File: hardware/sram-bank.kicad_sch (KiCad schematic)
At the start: 6 parts, among them U1 NAND, U13 decoder

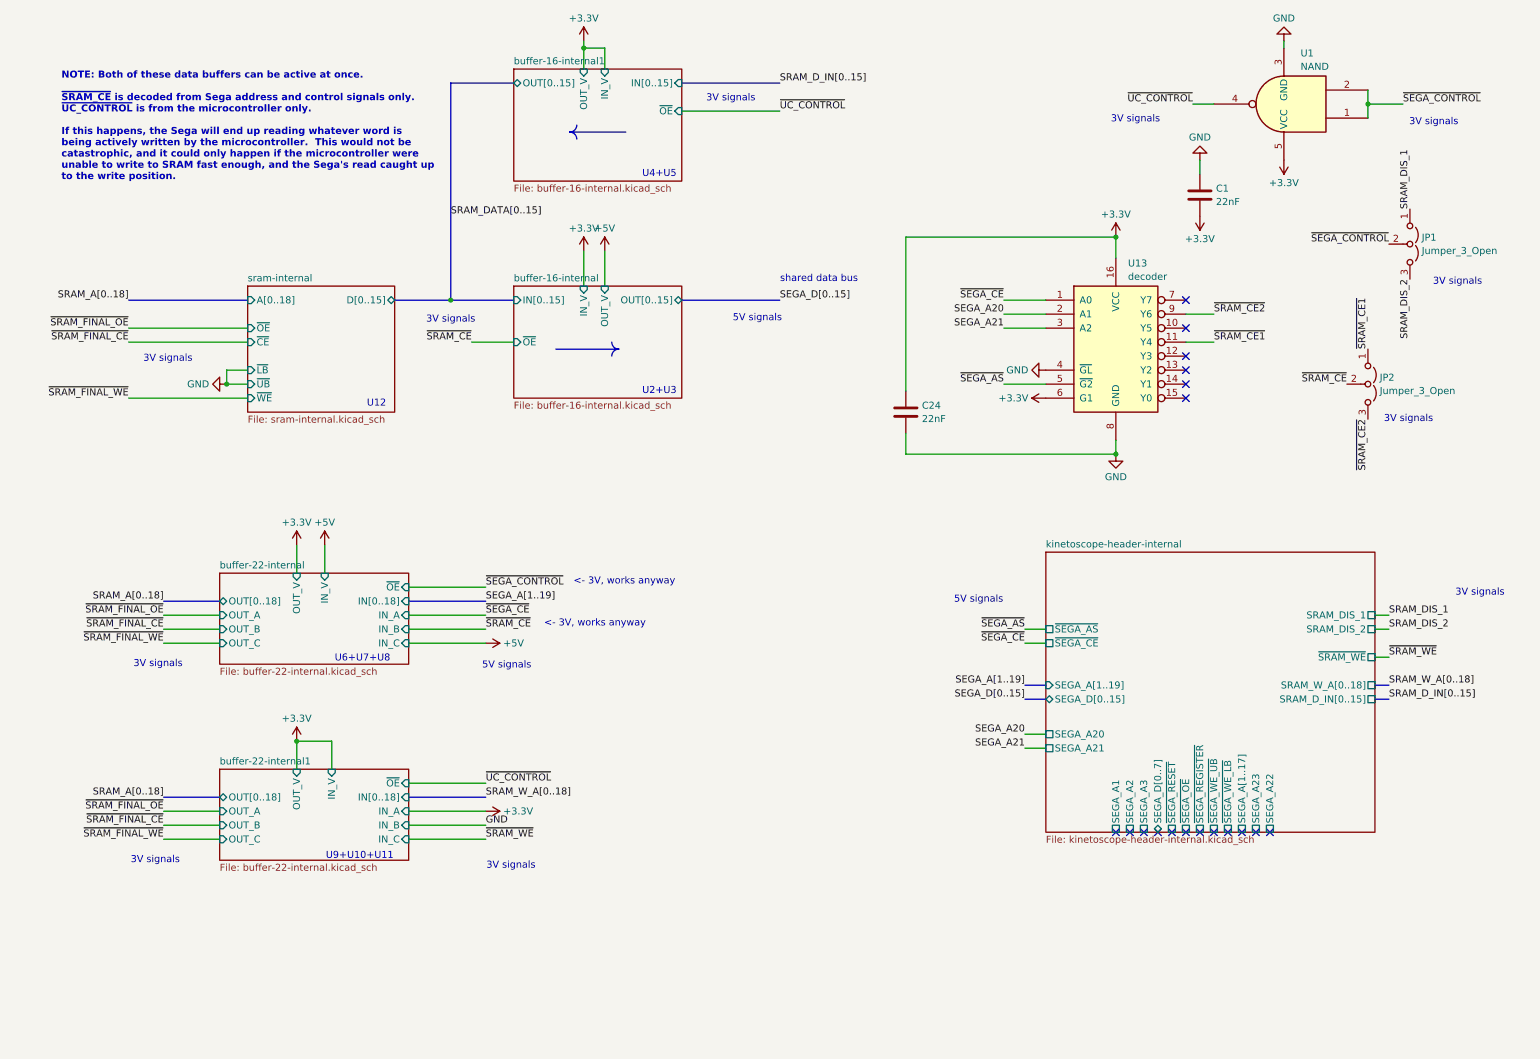
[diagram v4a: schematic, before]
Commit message: Redesign SRAM address decoders
 - Redo original address decoder for SRAM_CE signal
 - Replace NAND gate with another address decoder
   - Simplifies the BOM by removing a one-off part
   - Stabilizes the control signals by making sure SEGA_CONTROL and
     UC_CONTROL can never be active at once (one does not depend on
     the other)
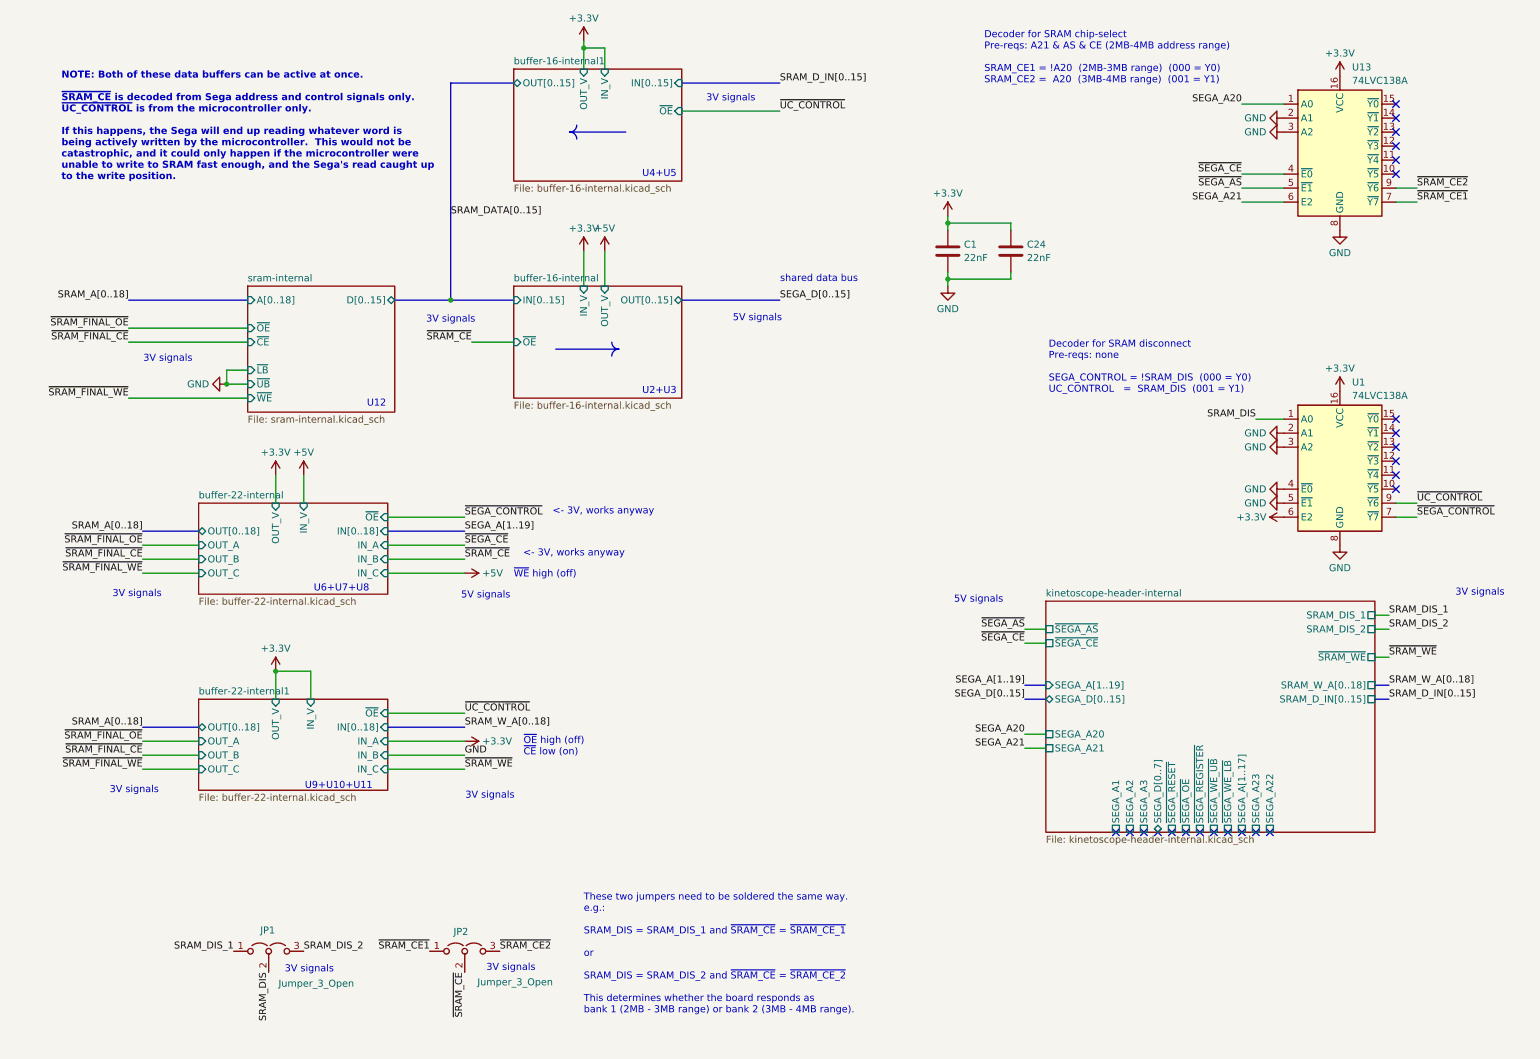
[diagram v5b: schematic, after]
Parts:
- removed U1: NAND, Package_TO_SOT_SMD:SC-74A-5_1.55x2.9mm_P0.95mm, symbol 74xGxx:SN74LVC1G00DRL
- added U1: 74LVC138A, Package_SO:TSSOP-16_4.4x5mm_P0.65mm, symbol 74xx:74HC138
- U13: value decoder -> 74LVC138A; footprint Package_SO:SO-16_3.9x9.9mm_P1.27mm -> Package_SO:TSSOP-16_4.4x5mm_P0.65mm; symbol 74xx:74LS137 -> 74xx:74HC138; JLCPCB Part Number C17116 -> C6062; Mouser Part Number 771-74HC137D-T -> 771-74LVC138APW-T; Part Number 74HC137D,653 -> 74LVC138APW,118
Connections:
- net +3.3V: now also C1.1, U1.16 (VCC), U1.6 (E2); no longer C1.2, U13.6 (G1)
- net GND: now also C1.2, U13.2 (A1), U13.3 (A2), U1.2 (A1), U1.3 (A2), U1.4 (~{E0}), U1.5 (~{E1}), U1.8 (GND); no longer C1.1, U13.4 (~{GL})
- net SEGA_A20: now also U13.1 (A0); no longer U13.2 (A1)
- net SEGA_A21: now also U13.6 (E2); no longer U13.3 (A2)
- net ~{SEGA_CE}: now also U13.4 (~{E0}); no longer U13.1 (A0)
- net ~{SEGA_CONTROL}: now also U1.7 (~{Y7}); no longer JP1.2 (C)
- net ~{SRAM_CE1}: now also U13.7 (~{Y7}); no longer U13.11 (Y4)
- net ~{UC_CONTROL}: now also U1.9 (~{Y6})
- new net SRAM_DIS: JP1.2 (C), U1.1 (A0)
- no-connect marks 18 -> 24
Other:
- note added: "Decoder for SRAM chip-select Pre-reqs: A21 & AS & CE (2MB-4MB address range) SRAM_CE1 = !A20 (2MB-3MB range) (000 = Y0) SRAM_CE2 = A20 (3MB-4MB range) (001 = Y1)"
- note added: "Decoder for SRAM disconnect Pre-reqs: none SEGA_CONTROL = !SRAM_DIS (000 = Y0) UC_CONTROL = SRAM_DIS (001 = Y1)"
- note added: "These two jumpers need to be soldered the same way. e.g.: SRAM_DIS = SRAM_DIS_1 and ~{SRAM_CE} = ~{SRAM_CE_1} or SRAM_DIS = SRAM_DIS_2 and ~{SRAM_CE} = ~{SRAM_CE_2} This determines whether the board responds as bank 1 (2MB - 3MB range) or bank 2 (3MB - 4MB range)."
- note added: "~{OE} high (off) ~{CE} low (on)"
- note added: "~{WE} high (off)"
- moved on the sheet: C1, JP1, JP2

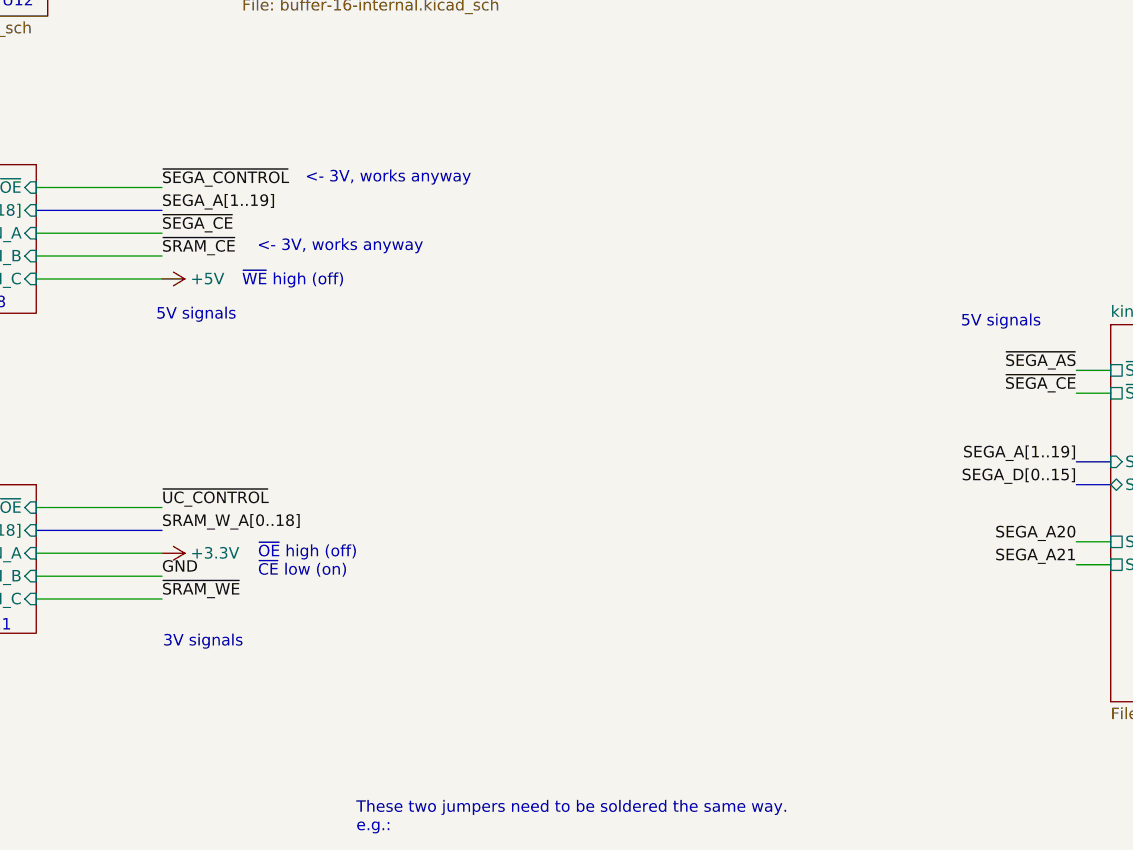
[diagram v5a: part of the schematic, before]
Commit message: Add test pads to SRAM board
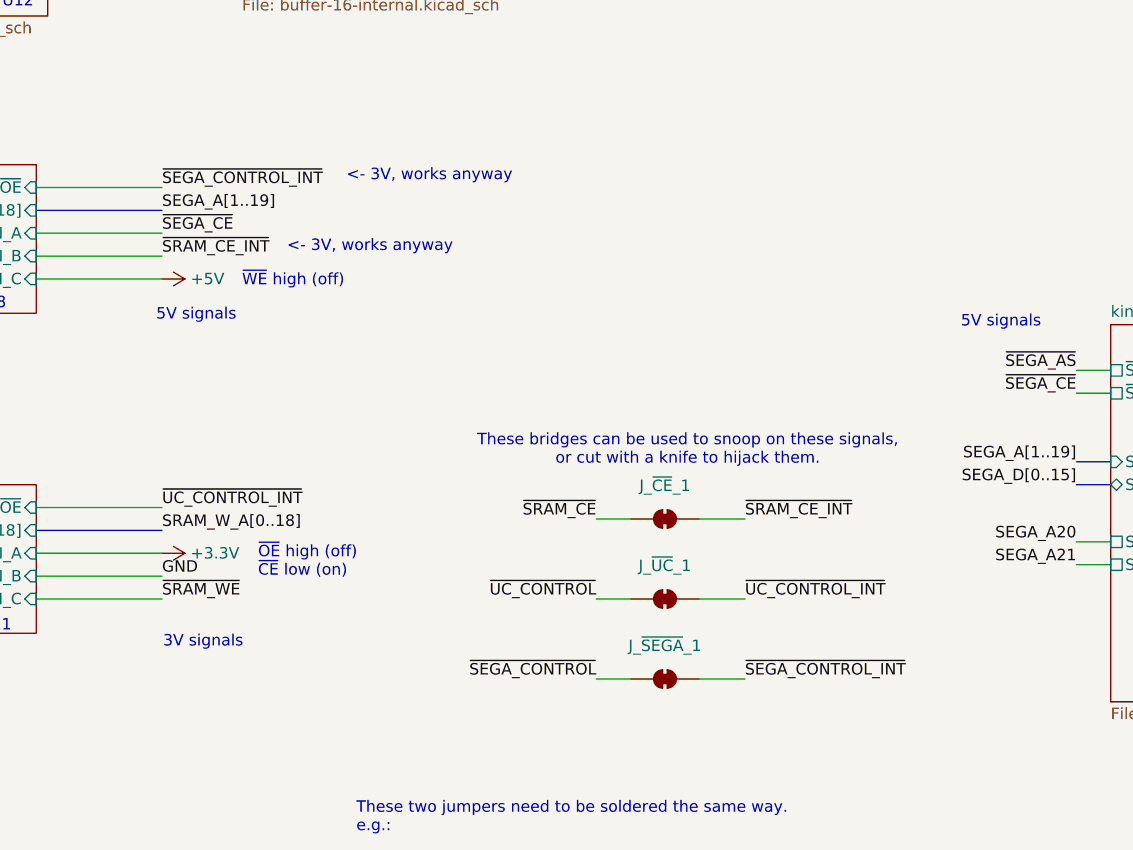
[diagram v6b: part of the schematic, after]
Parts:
- added J_~{CE}_1, J_~{SEGA}_1, J_~{UC}_1: ~, Jumper:SolderJumper-2_P1.3mm_Bridged_RoundedPad1.0x1.5mm, symbol Jumper:SolderJumper_2_Bridged
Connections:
- net ~{SEGA_CONTROL}: now also J_~{SEGA}_1.1 (A)
- net ~{SRAM_CE}: now also J_~{CE}_1.1 (A)
- net ~{UC_CONTROL}: now also J_~{UC}_1.1 (A)
- new net ~{SEGA_CONTROL_INT}: J_~{SEGA}_1.2 (B)
- new net ~{SRAM_CE_INT}: J_~{CE}_1.2 (B)
- new net ~{UC_CONTROL_INT}: J_~{UC}_1.2 (B)
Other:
- note added: "These bridges can be used to snoop on these signals, or cut with a knife to hijack them."

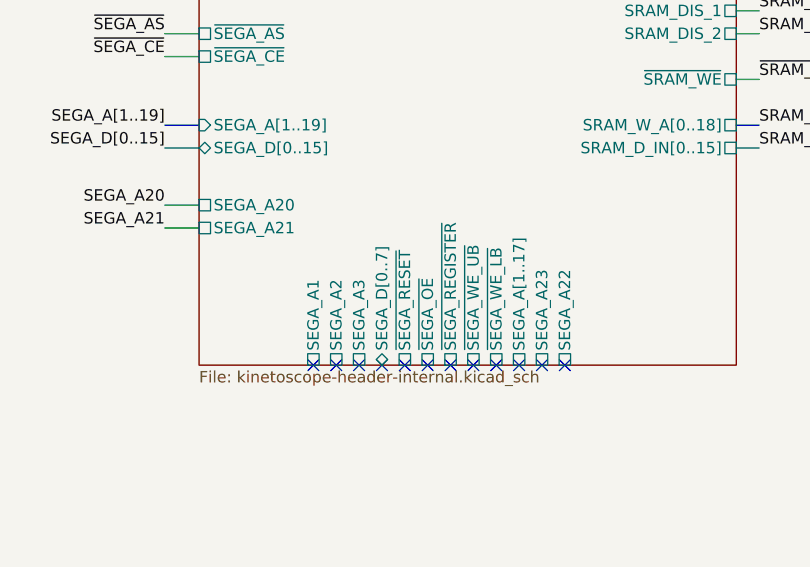
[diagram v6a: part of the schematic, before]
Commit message: Improve uC board assembly further
Change the register file CD74HC670M96 with SN74AHC373PWR and an
inverter, which is more easily available from JLCPCB.

This is not an exact replacement, as we replaced 2x 4x4 register files
with 2x 8-bit latches.  So instead of 4x 8-bit registers, we now only
have 2x 8-bit registers, but we only used 2 to begin with.

The new register hardware required us to change the address decoding
and the actual addresses of the registers.  Instead of 0xA13000 and
0xA13002, we now write to 0xA13010 and 0xA13012.
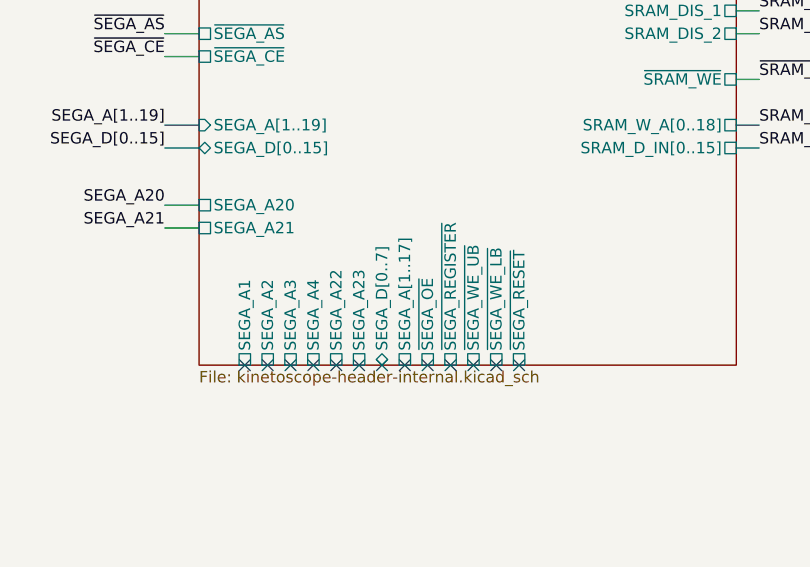
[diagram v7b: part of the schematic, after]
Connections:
- no-connect marks 24 -> 25
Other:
- sheet kinetoscope-header-internal ports: added SEGA_A4; removed none
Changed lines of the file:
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@@
 	)
 	(no_connect
+		(at 204.47 161.29)
+	)
+	(no_connect
 		(at 262.89 41.91)
 	)
@@
 	)
 	(no_connect
-		(at 237.49 161.29)
-	)
-	(no_connect
 		(at 262.89 99.06)
 	)
@@
 	)
 	(no_connect
-		(at 240.03 161.29)
-	)
-	(no_connect
 		(at 262.89 31.75)
 	)
@@
 	)
 	(no_connect
+		(at 209.55 161.29)
+	)
+	(no_connect
 		(at 232.41 161.29)
 	)
@@
 	)
 	(no_connect
+		(at 207.01 161.29)
+	)
+	(no_connect
 		(at 222.25 161.29)
 	)
@@
 		)
 		(pin "SEGA_A22" passive
-			(at 240.03 161.29 270)
+			(at 214.63 161.29 270)
 			(effects
 				(font
@@
 		)
 		(pin "SEGA_A23" passive
-			(at 237.49 161.29 270)
+			(at 217.17 161.29 270)
 			(effects
 				(font
@@
 		)
 		(pin "SEGA_A[1..17]" passive
-			(at 234.95 161.29 270)
+			(at 222.25 161.29 270)
 			(effects
 				(font
@@
 		)
 		(pin "~{SEGA_RESET}" passive
-			(at 222.25 161.29 270)
+			(at 234.95 161.29 270)
 			(effects
 				(font
@@
 		)
 		(pin "SEGA_A2" passive
-			(at 214.63 161.29 270)
+			(at 207.01 161.29 270)
 			(effects
 				(font
@@
 		)
 		(pin "SEGA_A1" passive
-			(at 212.09 161.29 270)
+			(at 204.47 161.29 270)
 			(effects
 				(font
@@
 		)
 		(pin "SEGA_A3" passive
-			(at 217.17 161.29 270)
+			(at 209.55 161.29 270)
 			(effects
 				(font
@@
 			(effects
 				(font
+					(size 1.27 1.27)
+				)
+				(justify left)
+			)
+		)
+		(pin "SEGA_A4" passive
+			(at 212.09 161.29 270)
+			(effects
+				(font

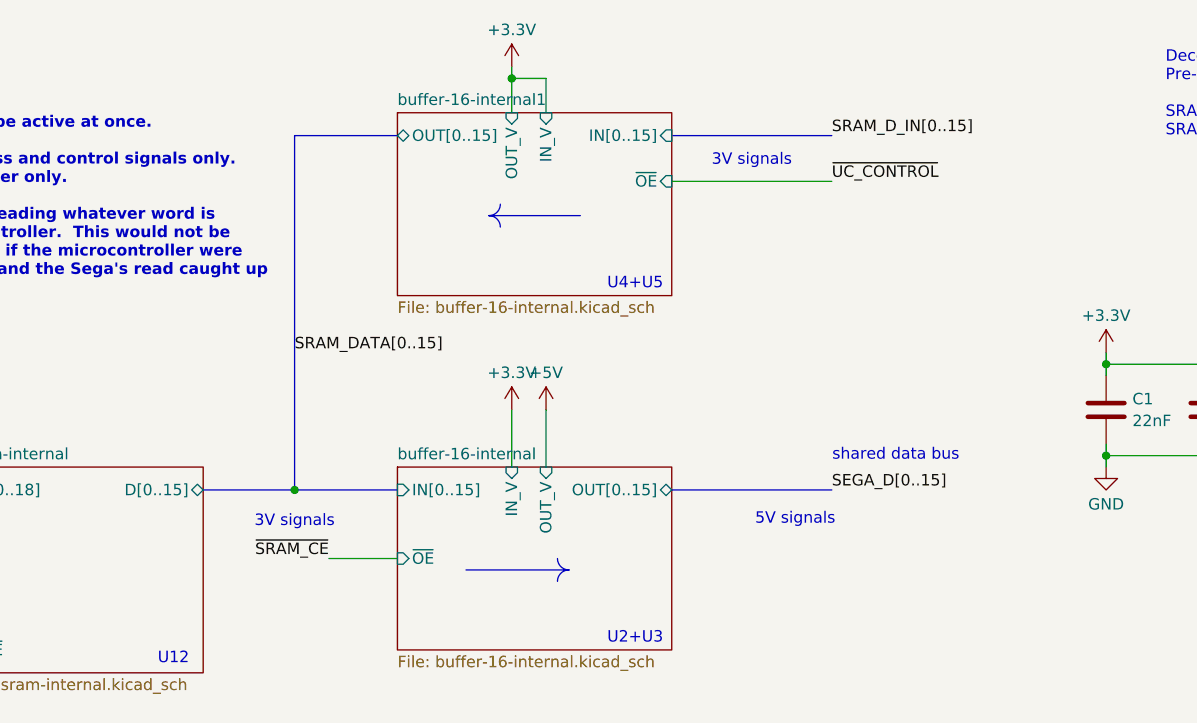
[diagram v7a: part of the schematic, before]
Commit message: Correct SRAM board debug pads
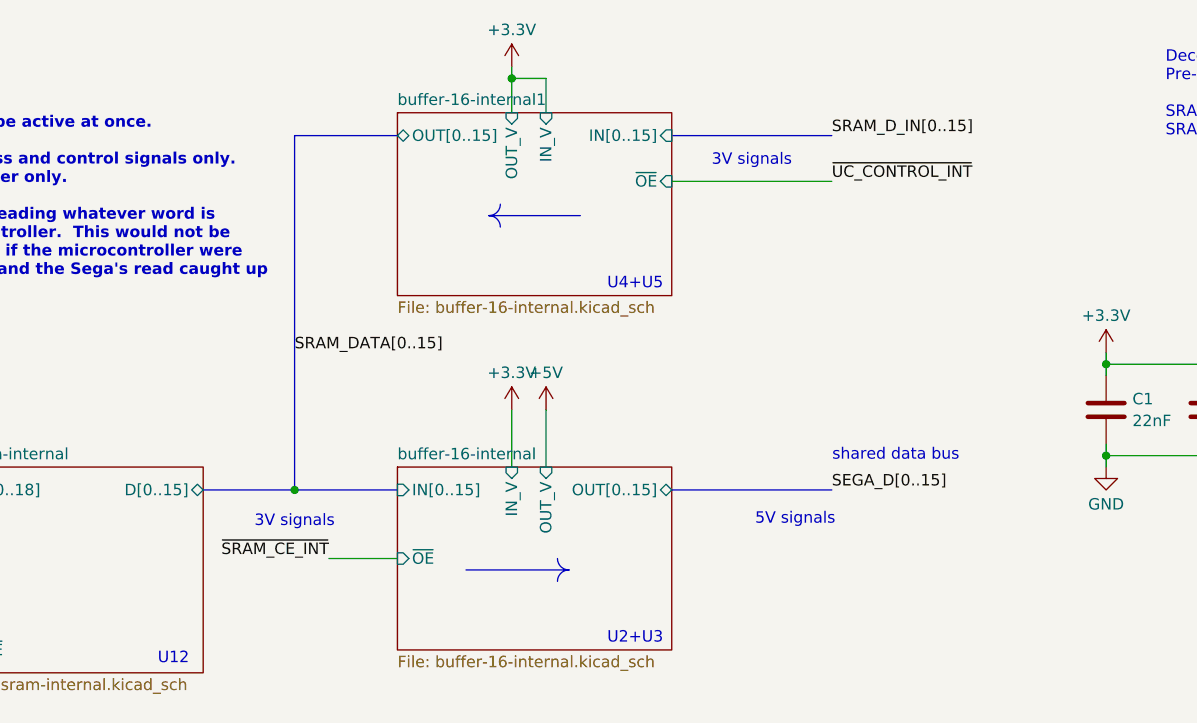
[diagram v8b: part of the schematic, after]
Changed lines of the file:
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@@
 		)
 	)
-	(label "~{UC_CONTROL}"
+	(label "~{UC_CONTROL_INT}"
 		(at 151.13 30.48 0)
 		(fields_autoplaced yes)
@@
 		)
 	)
-	(label "~{SRAM_CE}"
+	(label "~{SRAM_CE_INT}"
 		(at 95.25 72.39 180)
 		(fields_autoplaced yes)
